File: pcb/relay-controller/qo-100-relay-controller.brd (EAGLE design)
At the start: 85 x 83.8 mm, 125 parts, among them CON1 4P-SH-SIDE, CON10 2EDG-2P-5MM, CON11 2EDG-2P-5MM, CON12 2EDG-2P-5MM, CON13 2EDG-2P-5MM, CON14 2EDG-2P-5MM, CON2 2EDG-2P-5MM, CON3 2EDG-2P-5MM, CON4 2EDG-2P-5MM, CON5 2EDG-2P-5MM, CON6 2EDG-2P-5MM, CON7 2EDG-2P-5MM, CON8 2EDG-2P-5MM, CON9 2EDG-2P-5MM, Q1 AO3400, Q10 AO3400, Q11 AO3400, Q12 AO3400, Q2 AO3400, Q3 AO3400, Q4 AO3400, Q5 AO3400, Q6 AO3400, Q7 AO3400, Q8 AO3400, Q9 AO3400, U1 MCP1792-3.3, U2 MCP23017

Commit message: Nothing to do on Relay Controller
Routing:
- net R11: track 1.80 -> 50.2 mm, vias 0 -> 2
- net R5: track 1.80 -> 42.5 mm, vias 0 -> 2
- net R0: track 1.80 -> 38.1 mm, vias 0 -> 2
- net R10: track 1.80 -> 37.2 mm, vias 0 -> 2
- net R6: track 1.80 -> 28.7 mm, vias 0 -> 2
- net R4: track 1.80 -> 28.5 mm, vias 0 -> 2
- net R1: track 1.80 -> 27.4 mm, vias 0 -> 2
- net R9: track 1.80 -> 21.0 mm, vias 0 -> 2
- net R7: track 1.80 -> 16.7 mm, vias 0 -> 2
- net R2: track 1.80 -> 16.6 mm, vias 0 -> 2
- net R3: track 1.80 -> 15.4 mm, vias 0 -> 2
- net R8: track 1.80 -> 8.82 mm, vias 0 -> 2

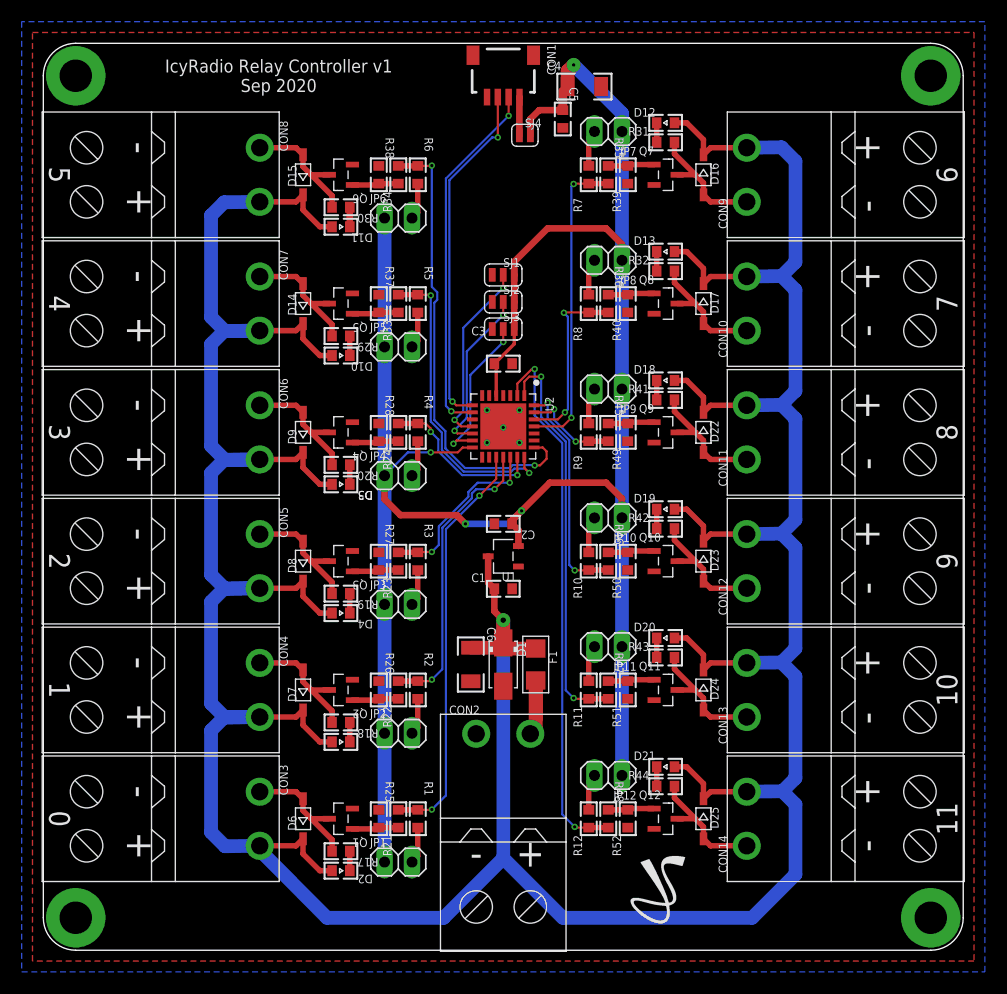
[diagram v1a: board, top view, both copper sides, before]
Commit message: Change IO expander to MCU in relay controller to allow later flexibility
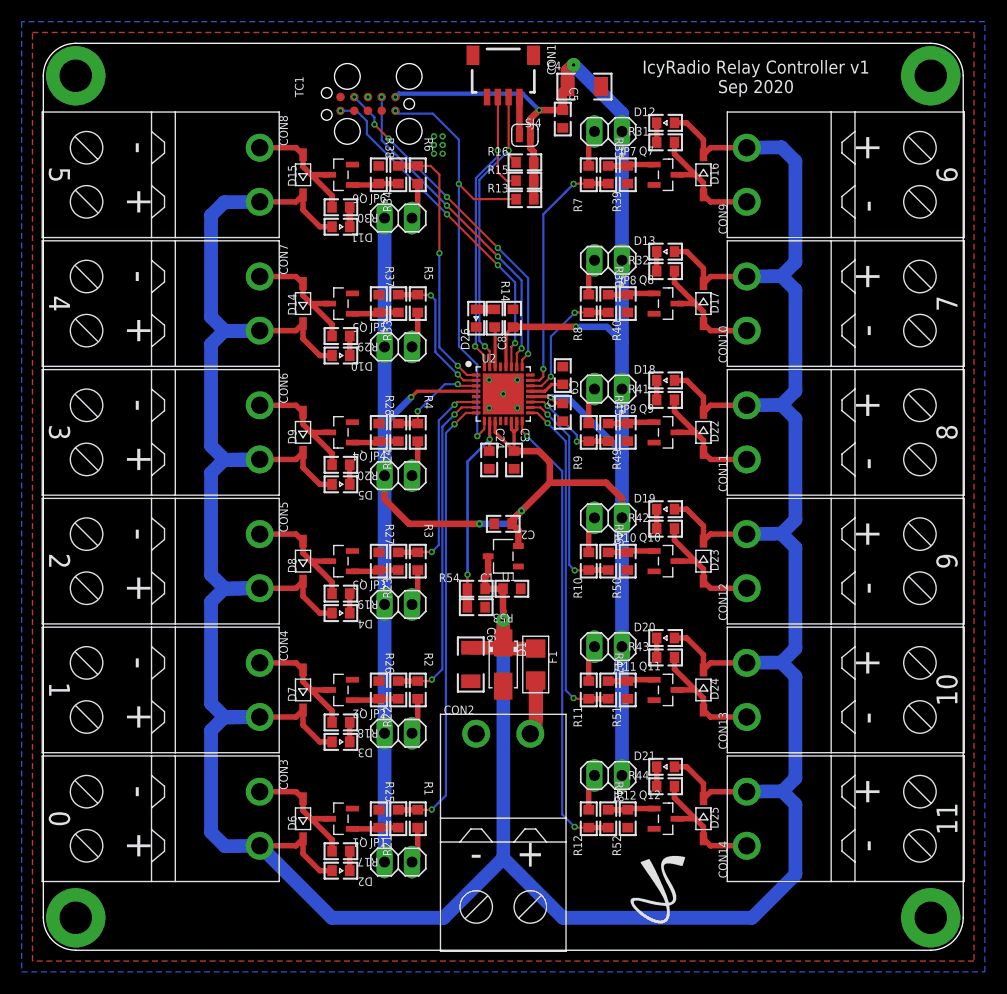
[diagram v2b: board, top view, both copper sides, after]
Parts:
- removed SJ1, SJ2, SJ3: (no value), Solder Jumper:SJ2_S
- added C24: 470pF, Capacitor:CAP0603
- added C7: 1uF, Capacitor:CAP0603
- added C8, C9: 100nF, Capacitor:CAP0603
- added D26: LED0603, LED:0603
- added R13, R53: 10K Ohms, Resistor:RES0603
- added R14: 330 Ohms, Resistor:RES0603
- added R15, R16: 1K Ohms, Resistor:RES0603
- added R54: 100K Ohms, Resistor:RES0603
- added TC1: TC2050-IDC, TagConnect:TC2050-IDC
- U2: value MCP23017 -> EFM32TG11B120F128GM32; device Microchip:QFN28 -> EFM32:QFN32_0.5P_TG
- moved C3 8.96 mm to (43.5, 45.3), turned to 270 degrees
- moved U2 3.00 mm to (42.5, 51.4), turned to 0 degrees
- moved C1 0.80 mm to (43.3, 33.4)
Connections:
- removed net IO_A0: SJ1.2, U2.11
- removed net IO_A1: SJ2.2, U2.12
- removed net IO_A2: SJ3.2, U2.13
- new net !RESET: R13.1, TC1.10, U2.9
- new net LED: R14.2, U2.30
- new net N$14: C7.1, U2.21
- new net N$15: D26.A, R14.1
- new net SWCLK: TC1.4, U2.25
- new net SWDIO: TC1.2, U2.26
- new net SWO: TC1.6, U2.27
- new net VIN_VSENSE: C24.1, R53.2, R54.1, U2.10
- net 3V3: now also C8.1, C9.1, R13.2, R15.2, R16.2, TC1.1, U2.11, U2.15, U2.20, U2.28, U2.4; no longer SJ1.3, SJ2.3, SJ3.3, U2.5
- net GND: now also C24.2, C7.2, C8.2, C9.2, D26.C, R53.1, TC1.3, U2.33; no longer SJ1.1, SJ2.1, SJ3.1, U2.29, U2.6
- net I2C_SCL: now also R15.1, U2.32; no longer U2.8
- net I2C_SDA: now also R16.1, U2.31; no longer U2.9
- net R0: now also U2.8; no longer U2.17
- net R1: now also U2.7; no longer U2.18
- net R10: now also U2.17; no longer U2.1
- net R11: now also U2.16; no longer U2.2
- net R2: now also U2.6; no longer U2.19
- net R3: now also U2.3; no longer U2.20
- net R4: now also U2.2; no longer U2.21
- net R5: now also U2.1; no longer U2.22
- net R6: now also U2.23; no longer U2.25
- net R7: now also U2.22; no longer U2.26
- net R8: now also U2.19; no longer U2.27
- net R9: now also U2.18; no longer U2.28
- net VIN: now also R54.2
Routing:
- net !RESET: track 0.00 -> 42.6 mm, vias 0 -> 3
- net 3V3: track 205.0 -> 239.2 mm, vias 4 -> 8
- net SWCLK: track 0.00 -> 31.8 mm, vias 0 -> 6
- net SWO: track 0.00 -> 31.4 mm, vias 0 -> 4
- net SWDIO: track 0.00 -> 30.5 mm, vias 0 -> 4
- net VIN_VSENSE: track 0.00 -> 19.2 mm, vias 0 -> 2
- net R5: track 42.5 -> 24.6 mm
- net IO_A0: track 17.2 -> 0.00 mm, vias 2 -> 0
- net IO_A1: track 15.5 -> 0.00 mm, vias 2 -> 0
- net R4: track 28.5 -> 13.3 mm
- net IO_A2: track 14.4 -> 0.00 mm, vias 2 -> 0
- net R11: track 50.2 -> 42.6 mm
- net R3: track 15.4 -> 9.43 mm
- net I2C_SDA: track 33.6 -> 27.8 mm
- net R10: track 37.2 -> 31.6 mm
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
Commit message: Work on PCBs
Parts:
- moved LOGO1 4.33 mm to (55.4, 7.50)

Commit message: Update I2C slave resistors to minimize load effect when powered down
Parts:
- R15, R16: value 1K Ohms -> 10K Ohms
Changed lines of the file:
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@@
 <drawing>
 <settings>
-<setting alwaysvectorfont="yes"/>
+<setting alwaysvectorfont="no"/>
 <setting verticaltext="up"/>
 </settings>
@@
 <attribute name="NAME" x="40.5" y="55.1" size="0.8" layer="25" font="vector" ratio="10" align="center-left"/>
 </element>
-<element name="R15" library="Resistor" package="RES0603" value="1K Ohms" x="44.5" y="71.1" smashed="yes">
+<element name="R15" library="Resistor" package="RES0603" value="10K Ohms" x="44.5" y="71.1" smashed="yes">
 <attribute name="NAME" x="40.7456" y="71.116" size="0.8" layer="25" font="vector" ratio="10" rot="SR0" align="center-left"/>
 <attribute name="TOLERANCE" value="" x="37.9" y="47.7" size="1.778" layer="27" display="off"/>
 <attribute name="VALUE" x="41.0456" y="69.068" size="0.8" layer="27" font="vector" ratio="10" rot="SR0" align="center-left"/>
 </element>
-<element name="R16" library="Resistor" package="RES0603" value="1K Ohms" x="44.5" y="72.8" smashed="yes">
+<element name="R16" library="Resistor" package="RES0603" value="10K Ohms" x="44.5" y="72.8" smashed="yes">
 <attribute name="NAME" x="40.7456" y="72.816" size="0.8" layer="25" font="vector" ratio="10" rot="SR0" align="center-left"/>
 <attribute name="TOLERANCE" value="" x="30.9" y="44.3" size="1.778" layer="27" display="off"/>
